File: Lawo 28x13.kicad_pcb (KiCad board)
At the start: 2 copper layers, 83.8 x 48.1 mm, 22 parts, among them IC1 FP2800a, J1 Solder_Jumper, J2 Solder_Jumper, J3 Solder_Jumper, J4 Solder_Jumper, J5 Solder_Jumper, J6 Solder_Jumper, U1 TSR-1

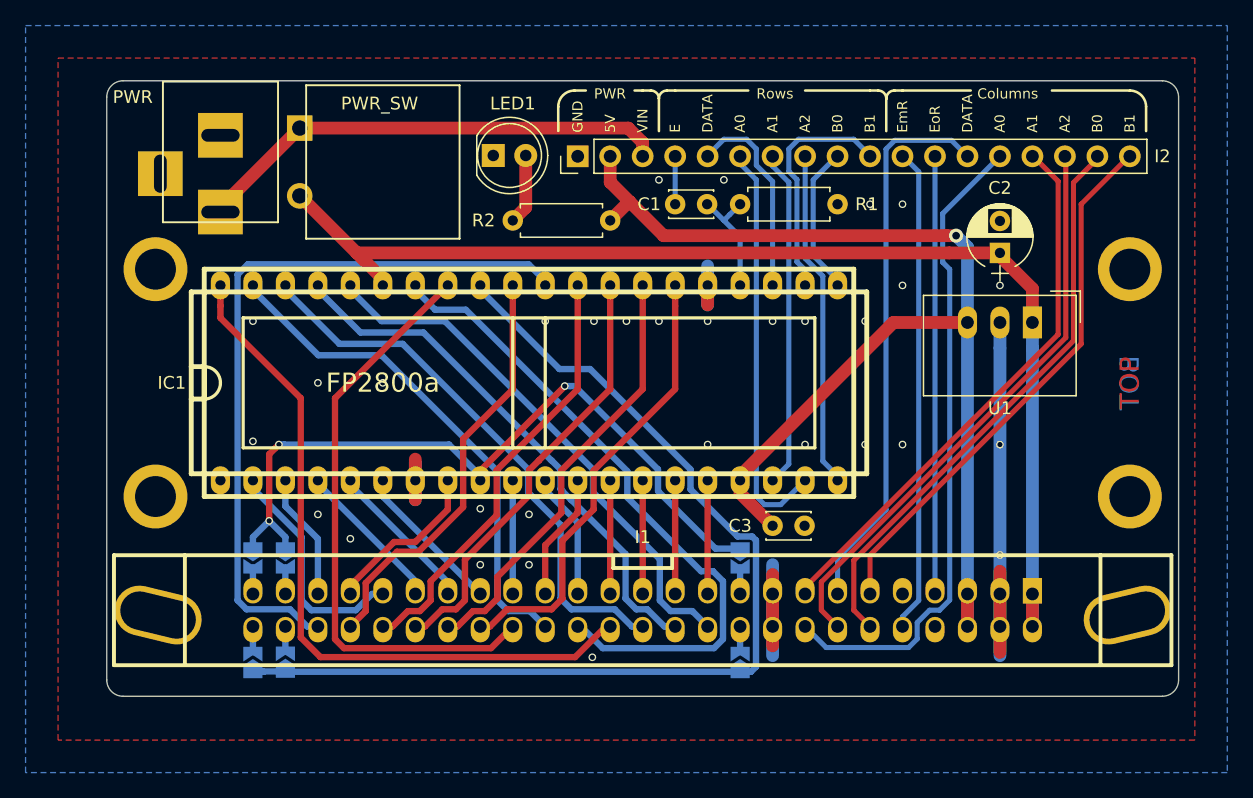
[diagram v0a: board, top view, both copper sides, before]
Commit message: Updated schematic for upgraded KiCad version and rework of many traces and pin assignments
- KiCad version upgrade
 - EESchema Schematic File Version 4
 - KiCad 5.0.0-rc3-dev
 - symbols and footprint exchanged to newer versions
- board changes
 - changed pin assignments for the set pins (swapped group of FP2800a 2a-g and 3a-g)
 - additional enable pins E_zR and E_yZ for spare connections
 - additional traces for one more set and one reset pin, routing to I1 selectable via solder jumper
 - increased trace widths
 - increased board size
 - silkscreen updates (outlines, component values, pin labels, ...)
 - bunch of vias added to shorten ground loops
- updated plots of the upgraded schematic, including images of the 3D viewer
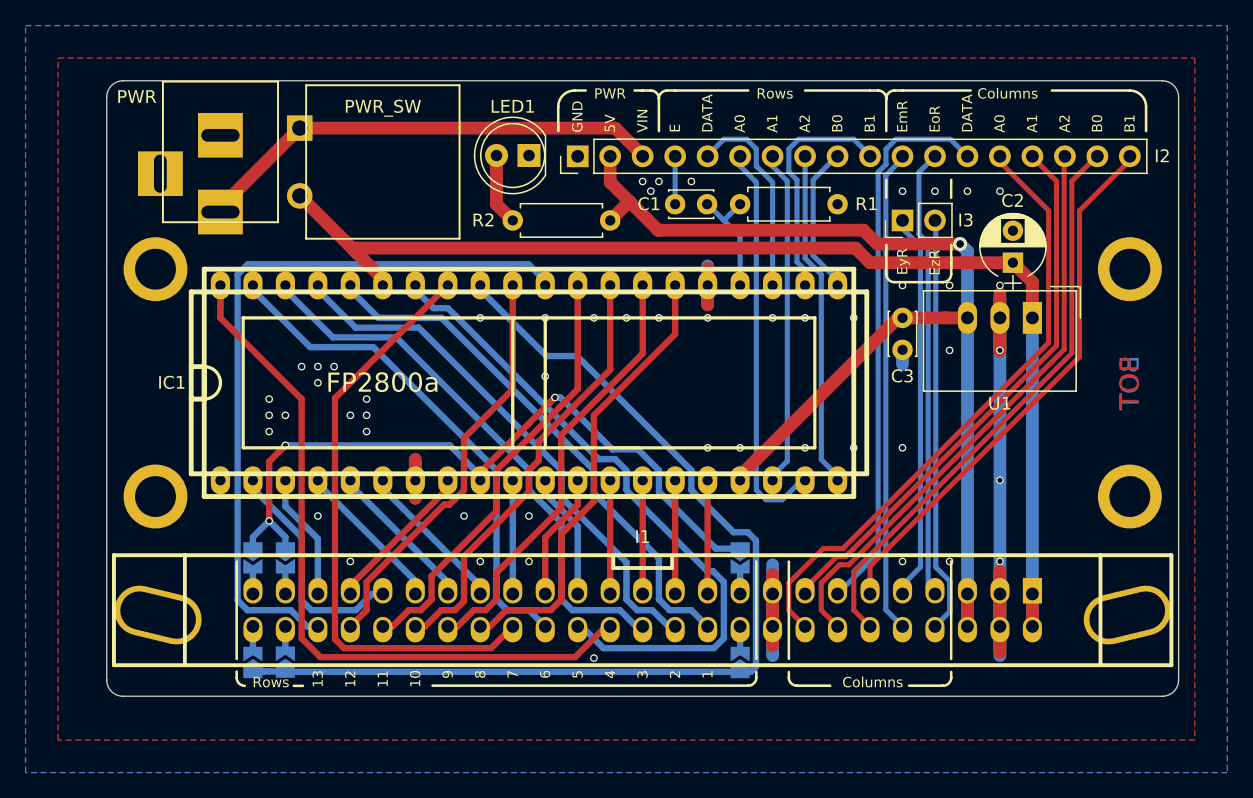
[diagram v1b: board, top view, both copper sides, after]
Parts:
- added I3: Spare Enable, Socket_Strips:Socket_Strip_Straight_1x02_Pitch2.54mm, F.Cu at (167.6, 99.1)
- C1: value 0.22uF -> 0.22μF
- C2: value 22uF -> 22μF
- moved C3 19.2 mm to (167.6, 106.7), turned to 270 degrees
- moved LED1 2.79 mm to (138.4, 94.0), turned to 180 degrees
- moved C2 1.27 mm to (176.3, 102.4)
- moved U1 0.36 mm to (177.8, 106.7)
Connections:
- I1 pad 8: Net-(I1-Pad8) -> COL_ENABLE_zR
- I1 pad 9: Net-(I1-Pad9) -> COL_ENABLE_yR
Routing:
- net COL_ENABLE_zR: track 0.00 -> 32.7 mm
- net COL_ENABLE_yR: track 0.00 -> 30.4 mm
- net GND: track 55.8 -> 64.4 mm, vias 31 -> 51
- net +5V: track 94.1 -> 89.5 mm
- net COL_A0: track 51.1 -> 48.2 mm
- net COL_A1: track 43.3 -> 44.8 mm
- net RESET_X: track 58.9 -> 57.6 mm
- net RESET_12: track 15.6 -> 14.6 mm
- net COL_ENABLE_oR: track 34.3 -> 35.3 mm
- net SET_12: track 32.9 -> 32.2 mm
- net ROW_A0: track 32.1 -> 31.4 mm
- net VIN: track 38.5 -> 37.9 mm
- net +24V: track 92.9 -> 93.4 mm
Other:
- net class GND added: clearance 0.2, trace_width 1, via_dia 0.9, via_drill 0.4
- net class POWER: via_dia 1.1 -> 0.9
- board text added: "EyR"
- board text added: "EzR"
- board text added: "Flip The Dot Lawo 28x13 Interface 1.1.0 February 2019 Robert Römer"
- board text added: "Value 0.22μF 22μF 0.1μF 15k 220 24V->5V"
- board text removed: "24V 1A"
- board text removed: "Flip The Dot Lawo 28x13 Flip Dot Interface 0.12 January 2019 Robert Römer"
- board text removed: "Todos: - check if Enable pins are on the correct side of the row - check if all FP2800a pins are connected in the right order - think about to add an additional 1x2 header with solder pads for the free pins on the opposite of EoR and EmR on I1 - Labels for the FP2800a IC pins? - move IC3 closer to U1?"
- board text removed: "Value 0.1μF 22μF 0.1μF 15k 220 24V->5V"
